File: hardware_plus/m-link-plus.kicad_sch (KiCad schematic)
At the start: 27 parts, among them J3 SIG, J4 PROGRAM, J5 I2C, SW1 RESTORE SETTINGS, U1 AP1117-33, U2 DRV8837C, U3 DRV8837C, U4 ESP-12F, U5 PCA9685PW, U6 DRV8837C

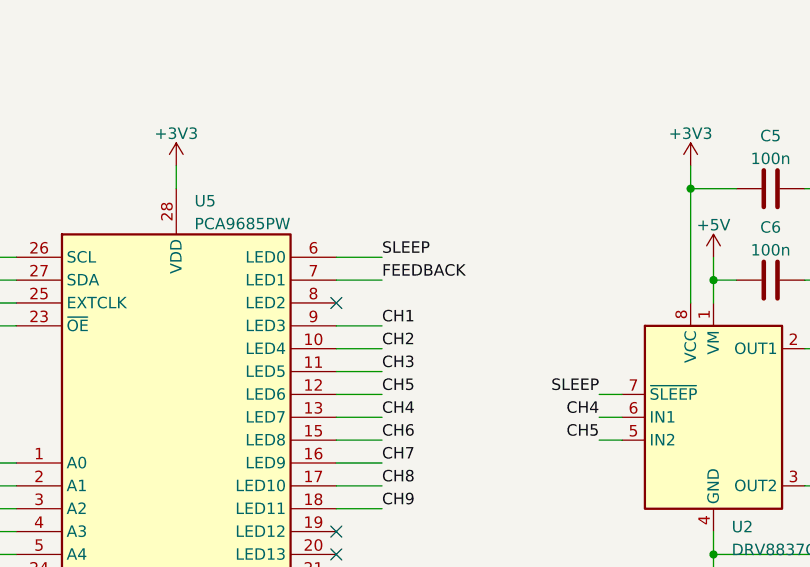
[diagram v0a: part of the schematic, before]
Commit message: Move feedback pin on the pca9685 to be adjacent to the servos.
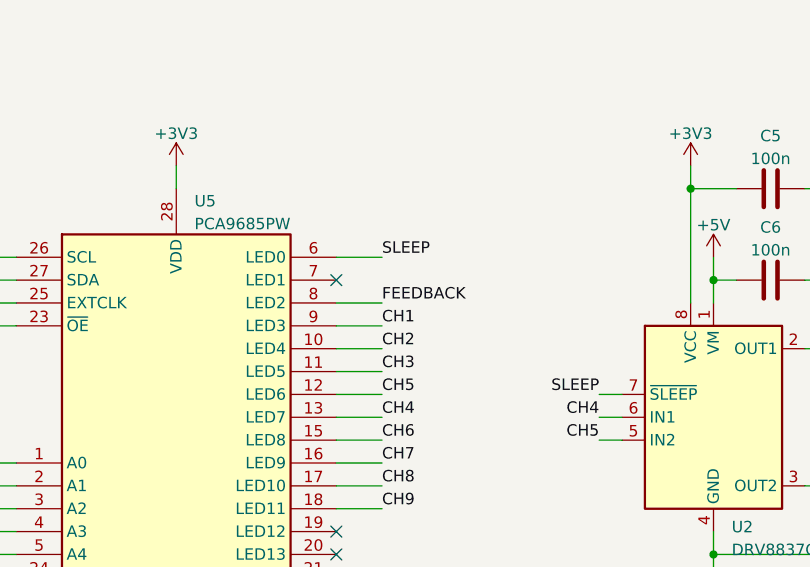
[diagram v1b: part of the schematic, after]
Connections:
- net FEEDBACK: now also U5.8 (LED2); no longer U5.7 (LED1)
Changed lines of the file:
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@@
   (no_connect (at 102.87 247.65))
   (no_connect (at 173.99 80.01))
+  (no_connect (at 102.87 217.17))
   (no_connect (at 143.51 74.93))
   (no_connect (at 102.87 252.73))
   (no_connect (at 143.51 87.63))
   (no_connect (at 143.51 82.55))
-  (no_connect (at 102.87 219.71))
   (no_connect (at 27.94 83.82))
   (no_connect (at 143.51 77.47))
@@
     (stroke (width 0) (type default) (color 0 0 0 0))
   )
-  (wire (pts (xy 102.87 217.17) (xy 107.95 217.17))
-    (stroke (width 0) (type default) (color 0 0 0 0))
-  )
   (wire (pts (xy 173.99 67.31) (xy 176.53 67.31))
     (stroke (width 0) (type default) (color 0 0 0 0))
@@
     (stroke (width 0) (type default) (color 0 0 0 0))
   )
+  (wire (pts (xy 102.87 219.71) (xy 107.95 219.71))
+    (stroke (width 0) (type default) (color 0 0 0 0))
+  )
   (wire (pts (xy 52.07 36.83) (xy 62.23 36.83))
     (stroke (width 0) (type default) (color 0 0 0 0))
@@
     (effects (font (size 1.27 1.27)) (justify left bottom))
   )
-  (label "FEEDBACK" (at 107.95 217.17 0)
-    (effects (font (size 1.27 1.27)) (justify left bottom))
-  )
+  (label "FEEDBACK" (at 107.95 219.71 0)
+    (effects (font (size 1.27 1.27)) (justify left bottom))
+  )

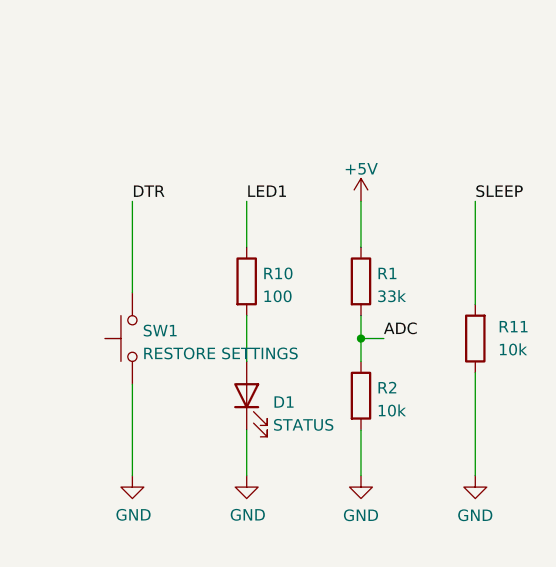
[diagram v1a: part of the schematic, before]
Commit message: Tidy up plus layout. Add plus HTML BOM.
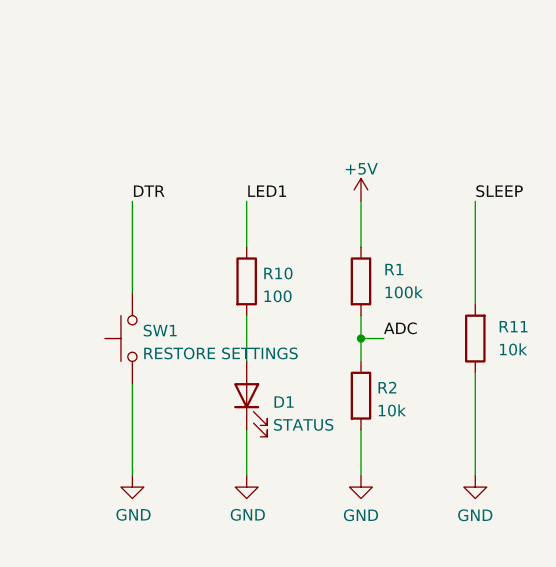
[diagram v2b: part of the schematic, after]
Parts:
- R1: value 33k -> 100k
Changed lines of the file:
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@@
   (symbol (lib_id "Device:R") (at 292.1 54.61 0) (unit 1)
     (in_bom yes) (on_board yes) (fields_autoplaced)
-    (property "Reference" "R1" (id 0) (at 293.878 53.7753 0)
-      (effects (font (size 1.27 1.27)) (justify left))
-    )
-    (property "Value" "33k" (id 1) (at 293.878 56.3122 0)
+    (property "Reference" "R1" (id 0) (at 294.64 53.3399 0)
+      (effects (font (size 1.27 1.27)) (justify left))
+    )
+    (property "Value" "100k" (id 1) (at 294.64 55.8799 0)
       (effects (font (size 1.27 1.27)) (justify left))
     )
@@
     )
     (path "/7aeeab49-3ed1-46e4-a03e-8fd112ecfd01"
-      (reference "R1") (unit 1) (value "33k") (footprint "Resistor_SMD:R_0603_1608Metric")
+      (reference "R1") (unit 1) (value "100k") (footprint "Resistor_SMD:R_0603_1608Metric")
     )
     (path "/c3aa991f-dbfb-4213-89e8-1b7194d21059"
